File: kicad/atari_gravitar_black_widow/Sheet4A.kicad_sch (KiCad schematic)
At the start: 14 parts

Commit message: reviewed first two sheets
see notes on individual sheets
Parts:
- added TPR/~{W}, TP~{ROM0}, TP~{ROM1}, TP~{ROM2}, TP~{ROM3}, TP~{ROM4}, TP~{ROM5}, TP~{VMEM}, TPΦ2: TP, symbol atari_grav_bw:TP
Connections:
- net ROM: no longer R_1.1 (B0)
- net R/~{W}: now also TPR/~{W}.1, TPR/~{W}.2
- net ~{ROM0}: now also TP~{ROM0}.1, TP~{ROM0}.2
- net ~{ROM1}: now also TP~{ROM1}.1, TP~{ROM1}.2
- net ~{ROM2}: now also TP~{ROM2}.1, TP~{ROM2}.2
- net ~{ROM3}: now also TP~{ROM3}.1, TP~{ROM3}.2
- net ~{ROM4}: now also TP~{ROM4}.1, TP~{ROM4}.2
- net ~{ROM5}: now also TP~{ROM5}.1, TP~{ROM5}.2
- net Φ2: now also TPΦ2.1, TPΦ2.2
- net LATCH renamed ~{LATCH}
- net ~{I/O5} renamed ~{I/OS}
- new net ~{VMEM}: R_1.1 (B0), TP~{VMEM}.1, TP~{VMEM}.2
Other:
- note added: "1/14 (am): renamed IO5 to IOS changed R4 to DeMorgan alt fixed internal labels of 6502 changed LATCH to ~{LATCH} (but not sure where that goes!) added test points off R1"

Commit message: Fri Night
various reviews
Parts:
- removed R_4: LS00, symbol Asteroids:LS00
- added R4: LS32, symbol atari_grav_bw:LS32
- renumbered B_1 to B1, C_1 to C1, C_2 to C2, F_2 to F2, F_3 to F3, J_3 to J3, J_4 to J4, K_4 to K4, P_3 to P3, R_1 to R1, R_2 to R2, TPΦ2 to TPPHI2
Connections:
- net ROM: now also R4.1
- net ~{I/OS}: now also R4.2
- net at F2.19 (CE): now also R4.3
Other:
- note added: "Address Decoder"
- note added: "Microprocessor"
- note removed: "1/14 (am): renamed IO5 to IOS changed R4 to DeMorgan alt fixed internal labels of 6502 changed LATCH to ~{LATCH} (but not sure where that goes!) added test points off R1"
- note removed: "ADDRESS DECODER"
- note removed: "MIROPROCESSOR"

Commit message: 20 errors left
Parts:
- renumbered C1 to C_1, C2 to C_2, R1 to R_1, R2 to R_2, R4 to R_4
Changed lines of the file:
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@@
   (symbol (lib_id "atari_grav_bw:6502") (at 121.92 191.77 0) (unit 1)
     (in_bom yes) (on_board yes)
-    (property "Reference" "C2" (id 0) (at 119.634 186.078 0)
+    (property "Reference" "C_2" (id 0) (at 119.634 186.078 0)
       (effects (font (size 1.524 1.524)) (justify left))
     )
@@
   (symbol (lib_id "atari_grav_bw:LS32") (at 178.435 280.67 0) (mirror x) (unit 1)
     (in_bom yes) (on_board yes)
-    (property "Reference" "R4" (id 0) (at 178.435 279.4 0))
+    (property "Reference" "R_4" (id 0) (at 178.435 279.4 0))
     (property "Value" "LS32" (id 1) (at 178.435 281.94 0))
     (property "Footprint" "" (id 2) (at 178.435 280.67 0)
@@
   (symbol (lib_name "136010-X_1") (lib_id "atari_grav_bw:136010-X") (at 455.93 242.57 0) (unit 1)
     (in_bom yes) (on_board yes)
-    (property "Reference" "R1" (id 0) (at 453.644 250.317 0)
+    (property "Reference" "R_1" (id 0) (at 453.644 250.317 0)
       (effects (font (size 1.27 1.27)) (justify left))
     )
@@
   (symbol (lib_id "atari_grav_bw:LS244A") (at 210.058 173.99 0) (unit 1)
     (in_bom yes) (on_board yes)
-    (property "Reference" "C1" (id 0) (at 208.026 165.735 0)
+    (property "Reference" "C_1" (id 0) (at 208.026 165.735 0)
       (effects (font (size 1.27 1.27)) (justify left))
     )
@@
   (symbol (lib_id "atari_grav_bw:136010-X") (at 455.676 91.948 0) (unit 1)
     (in_bom yes) (on_board yes)
-    (property "Reference" "R2" (id 0) (at 453.263 98.806 0)
-      (effects (font (size 1.27 1.27)) (justify left))
-    )
+    (property "Reference" "R_2" (id 0) (at 453.263 98.806 0)
+      (effects (font (size 1.27 1.27)) (justify left))
+    )

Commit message: Fixed most errors
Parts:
- renumbered TPR/~{W} to TPR/~{W}1, TP~{ROM0} to TP~{ROM0}1, TP~{ROM1} to TP~{ROM1}1, TP~{ROM2} to TP~{ROM2}1, TP~{ROM3} to TP~{ROM3}1, TP~{ROM4} to TP~{ROM4}1, TP~{ROM5} to TP~{ROM5}1, TP~{VMEM} to TP~{VMEM}1
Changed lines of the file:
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@@
   (symbol (lib_id "atari_grav_bw:TP") (at 344.805 66.675 0) (unit 1)
     (in_bom yes) (on_board yes)
-    (property "Reference" "TPR/~{W}" (id 0) (at 347.8276 66.8782 0)
+    (property "Reference" "TPR/~{W}1" (id 0) (at 347.8276 66.8782 0)
       (effects (font (size 1.524 1.524)) (justify left))
     )
@@
   (symbol (lib_id "atari_grav_bw:TP") (at 563.245 292.1 0) (unit 1)
     (in_bom yes) (on_board yes)
-    (property "Reference" "TP~{ROM4}" (id 0) (at 566.2676 292.3032 0)
+    (property "Reference" "TP~{ROM4}1" (id 0) (at 566.2676 292.3032 0)
       (effects (font (size 1.524 1.524)) (justify left))
     )
@@
   (symbol (lib_id "atari_grav_bw:TP") (at 546.735 271.145 0) (unit 1)
     (in_bom yes) (on_board yes)
-    (property "Reference" "TP~{ROM1}" (id 0) (at 549.7576 271.3482 0)
+    (property "Reference" "TP~{ROM1}1" (id 0) (at 549.7576 271.3482 0)
       (effects (font (size 1.524 1.524)) (justify left))
     )
@@
   (symbol (lib_id "atari_grav_bw:TP") (at 546.735 257.175 0) (unit 1)
     (in_bom yes) (on_board yes)
-    (property "Reference" "TP~{VMEM}" (id 0) (at 549.7576 257.3782 0)
+    (property "Reference" "TP~{VMEM}1" (id 0) (at 549.7576 257.3782 0)
       (effects (font (size 1.524 1.524)) (justify left))
     )
@@
   (symbol (lib_id "atari_grav_bw:TP") (at 563.245 264.16 0) (unit 1)
     (in_bom yes) (on_board yes)
-    (property "Reference" "TP~{ROM0}" (id 0) (at 566.2676 264.3632 0)
+    (property "Reference" "TP~{ROM0}1" (id 0) (at 566.2676 264.3632 0)
       (effects (font (size 1.524 1.524)) (justify left))
     )
@@
   (symbol (lib_id "atari_grav_bw:TP") (at 546.735 299.085 0) (unit 1)
     (in_bom yes) (on_board yes)
-    (property "Reference" "TP~{ROM5}" (id 0) (at 549.7576 299.2882 0)
+    (property "Reference" "TP~{ROM5}1" (id 0) (at 549.7576 299.2882 0)
       (effects (font (size 1.524 1.524)) (justify left))
     )
@@
   (symbol (lib_id "atari_grav_bw:TP") (at 563.245 278.13 0) (unit 1)
     (in_bom yes) (on_board yes)
-    (property "Reference" "TP~{ROM2}" (id 0) (at 566.2676 278.3332 0)
+    (property "Reference" "TP~{ROM2}1" (id 0) (at 566.2676 278.3332 0)
       (effects (font (size 1.524 1.524)) (justify left))
     )
@@
   (symbol (lib_id "atari_grav_bw:TP") (at 546.735 285.115 0) (unit 1)
     (in_bom yes) (on_board yes)
-    (property "Reference" "TP~{ROM3}" (id 0) (at 549.7576 285.3182 0)
-      (effects (font (size 1.524 1.524)) (justify left))
-    )
+    (property "Reference" "TP~{ROM3}1" (id 0) (at 549.7576 285.3182 0)
+      (effects (font (size 1.524 1.524)) (justify left))
+    )

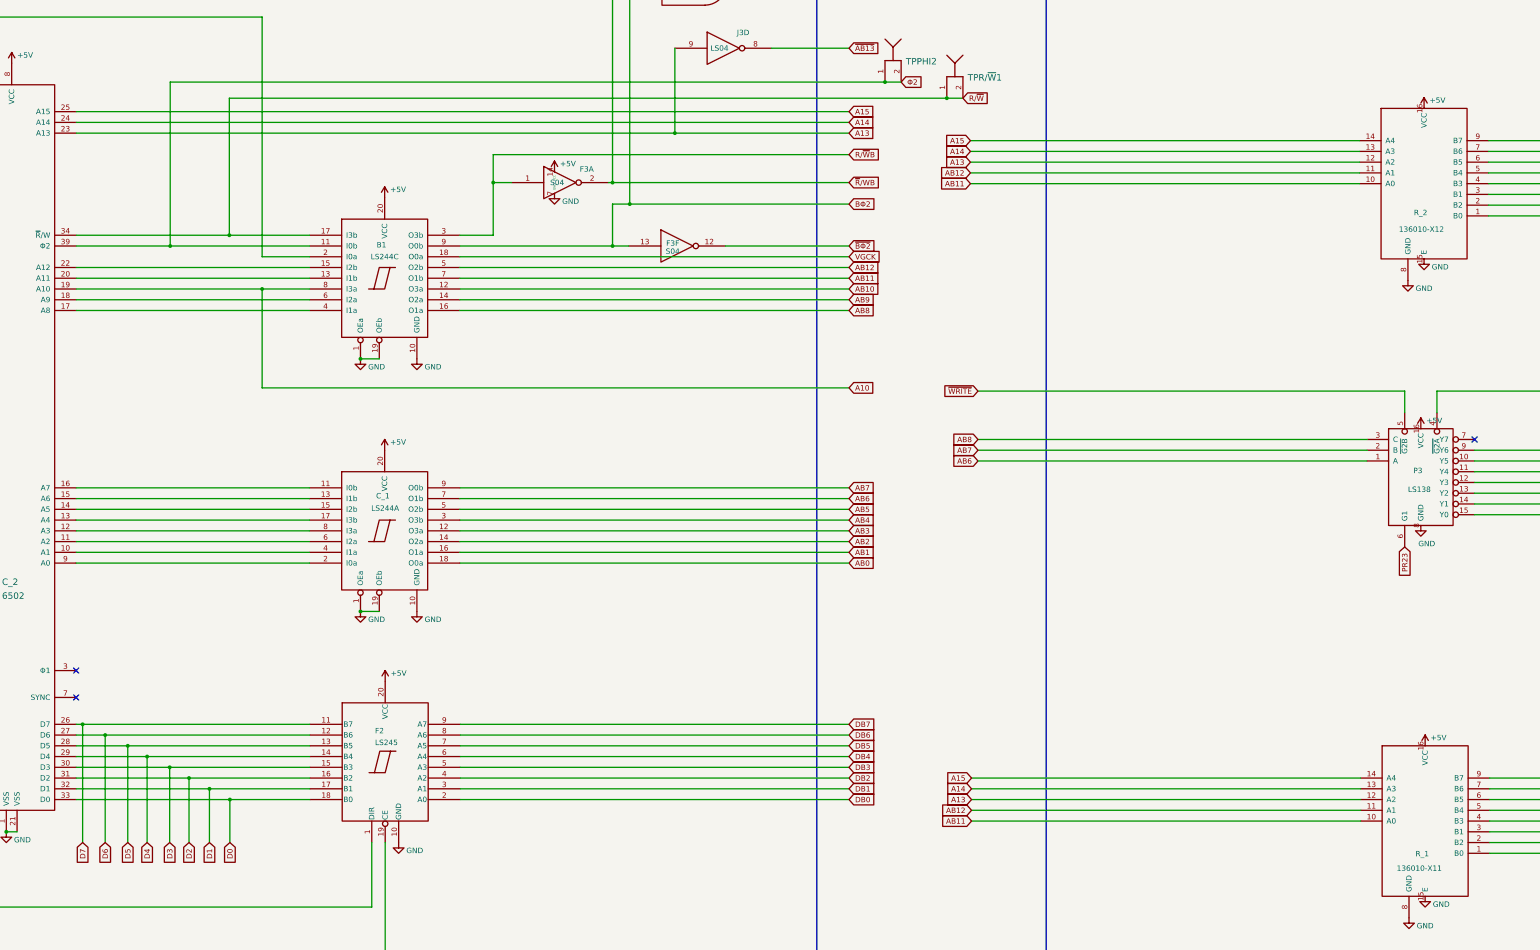
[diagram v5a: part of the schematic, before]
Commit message: Worked on removing the warnings
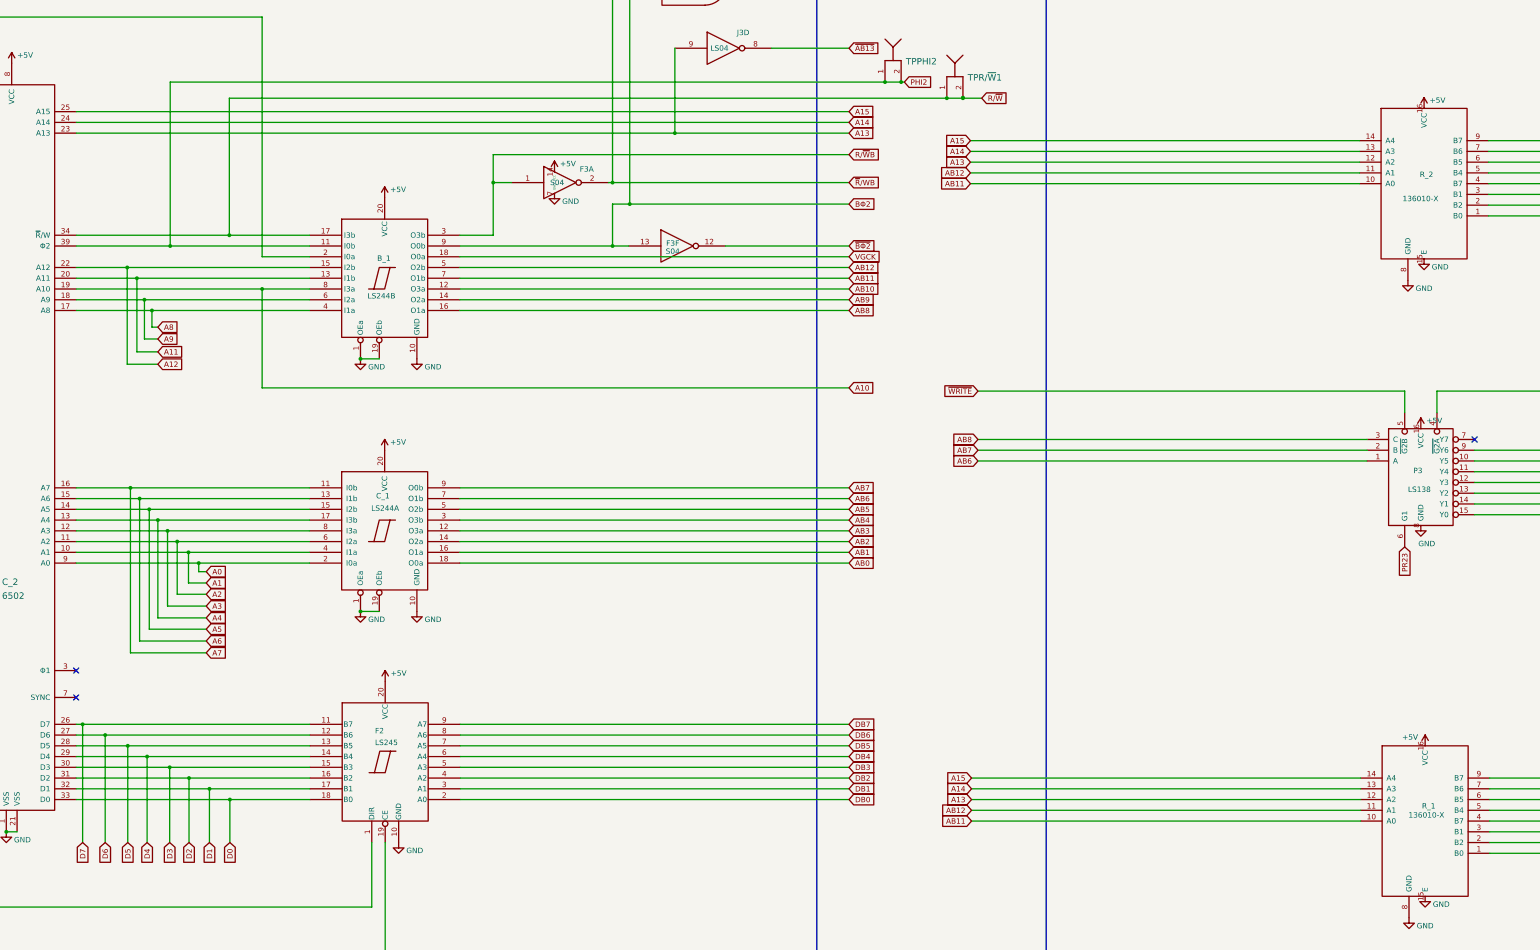
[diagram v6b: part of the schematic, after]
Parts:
- removed B1: LS244C, symbol atari_grav_bw:LS244C
- added B_1: LS244B, symbol atari_grav_bw:LS244B
- R_1: value 136010-X11 -> 136010-X
- R_2: value 136010-X12 -> 136010-X
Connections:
- net +5V: now also B_1.20 (VCC)
- net 1.5MHZ: now also B_1.2 (I0a)
- net A10: now also B_1.8 (I3a)
- net AB10: now also B_1.12 (O3a)
- net AB11: now also B_1.7 (O1b)
- net AB12: now also B_1.5 (O2b)
- net AB8: now also B_1.16 (O1a)
- net AB9: now also B_1.14 (O2a)
- net BΦ2: now also B_1.9 (O0b)
- net GND: now also B_1.1 (OEa), B_1.10 (GND), B_1.19 (OEb)
- net R/~{W}: now also B_1.17 (I3b)
- net R/~{W}B: now also B_1.3 (O3b)
- net VGCK: now also B_1.18 (O0a)
- net A1: now reaches C_1.4 (I1a), C_2.10 (A1)
- net A2: now reaches C_1.6 (I2a), C_2.11 (A2)
- net A3: now reaches C_1.8 (I3a), C_2.12 (A3)
- net A4: now reaches C_1.17 (I3b), C_2.13 (A4)
- net A5: now reaches C_1.15 (I2b), C_2.14 (A5)
- net A6: now reaches C_1.13 (I1b), C_2.15 (A6)
- net A7: now reaches C_1.11 (I0b), C_2.16 (A7)
- net A8: now reaches C_2.17 (A8)
- net A8: now also B_1.4 (I1a)
- net A9: now reaches C_2.18 (A9)
- net A9: now also B_1.6 (I2a)
- net A11: now reaches C_2.20 (A11)
- net A11: now also B_1.13 (I1b)
- net A12: now reaches C_2.22 (A12)
- net A12: now also B_1.15 (I2b)
- net A0: now reaches C_1.2 (I0a), C_2.9 (A0)
- net Φ2 renamed PHI2
- net PHI2: now also B_1.11 (I0b)

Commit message: Removed more warnings - 25 warnings remain
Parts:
- R19: footprint quantum_arcade_pcb:GenComp -> (none)

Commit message: Fixed all warnings and errors
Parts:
- renumbered F2 to F_2, F3 to F_3, J3 to J_3, J4 to J_4, K4 to K_4, P3 to P_3
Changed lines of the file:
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@@
   (symbol (lib_id "quantum_arcade_pcb:LS138") (at 454.914 161.29 0) (unit 1)
     (in_bom yes) (on_board yes)
-    (property "Reference" "P3" (id 0) (at 453.136 159.766 0)
+    (property "Reference" "P_3" (id 0) (at 453.136 159.766 0)
       (effects (font (size 1.27 1.27)) (justify left))
     )
@@
   (symbol (lib_id "atari_grav_bw:LS04") (at 251.46 91.694 0) (unit 1)
     (in_bom yes) (on_board yes)
-    (property "Reference" "F3" (id 0) (at 257.81 88.519 0))
+    (property "Reference" "F_3" (id 0) (at 257.81 88.519 0))
     (property "Value" "S04" (id 1) (at 250.825 91.694 0))
     (property "Footprint" "" (id 2) (at 251.46 91.694 0)
@@
   (symbol (lib_id "atari_grav_bw:LS245") (at 210.185 228.6 0) (unit 1)
     (in_bom yes) (on_board yes)
-    (property "Reference" "F2" (id 0) (at 207.772 221.2529 0)
+    (property "Reference" "F_2" (id 0) (at 207.772 221.2529 0)
       (effects (font (size 1.27 1.27)) (justify left))
     )
@@
   (symbol (lib_id "atari_grav_bw:LS10") (at 283.21 44.704 0) (unit 2)
     (in_bom yes) (on_board yes)
-    (property "Reference" "K4" (id 0) (at 283.337 42.037 0))
+    (property "Reference" "K_4" (id 0) (at 283.337 42.037 0))
     (property "Value" "S10" (id 1) (at 283.337 45.085 0))
     (property "Footprint" "" (id 2) (at 283.21 44.704 0)
@@
   (symbol (lib_id "atari_grav_bw:LS04") (at 279.146 106.68 0) (unit 6)
     (in_bom yes) (on_board yes)
-    (property "Reference" "F3" (id 0) (at 278.13 106.045 0))
+    (property "Reference" "F_3" (id 0) (at 278.13 106.045 0))
     (property "Value" "S04" (id 1) (at 278.13 107.95 0))
     (property "Footprint" "" (id 2) (at 279.146 106.68 0)
@@
   (symbol (lib_id "Asteroids:LS04") (at 290.068 59.944 0) (unit 4)
     (in_bom yes) (on_board yes)
-    (property "Reference" "J3" (id 0) (at 294.767 56.261 0))
+    (property "Reference" "J_3" (id 0) (at 294.767 56.261 0))
     (property "Value" "LS04" (id 1) (at 289.179 59.944 0))
     (property "Footprint" "" (id 2) (at 290.068 59.944 0)
@@
   (symbol (lib_id "Asteroids:LS161") (at 75.438 231.394 0) (unit 1)
     (in_bom yes) (on_board yes)
-    (property "Reference" "J4" (id 0) (at 75.184 229.362 0)
+    (property "Reference" "J_4" (id 0) (at 75.184 229.362 0)
       (effects (font (size 1.524 1.524)))
     )
